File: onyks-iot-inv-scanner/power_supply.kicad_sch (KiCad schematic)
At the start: 16 parts, among them Q1 DMN3150L, Q2 DMN3150L, U1 DW01A, U3 TP4056-42-ESOP8

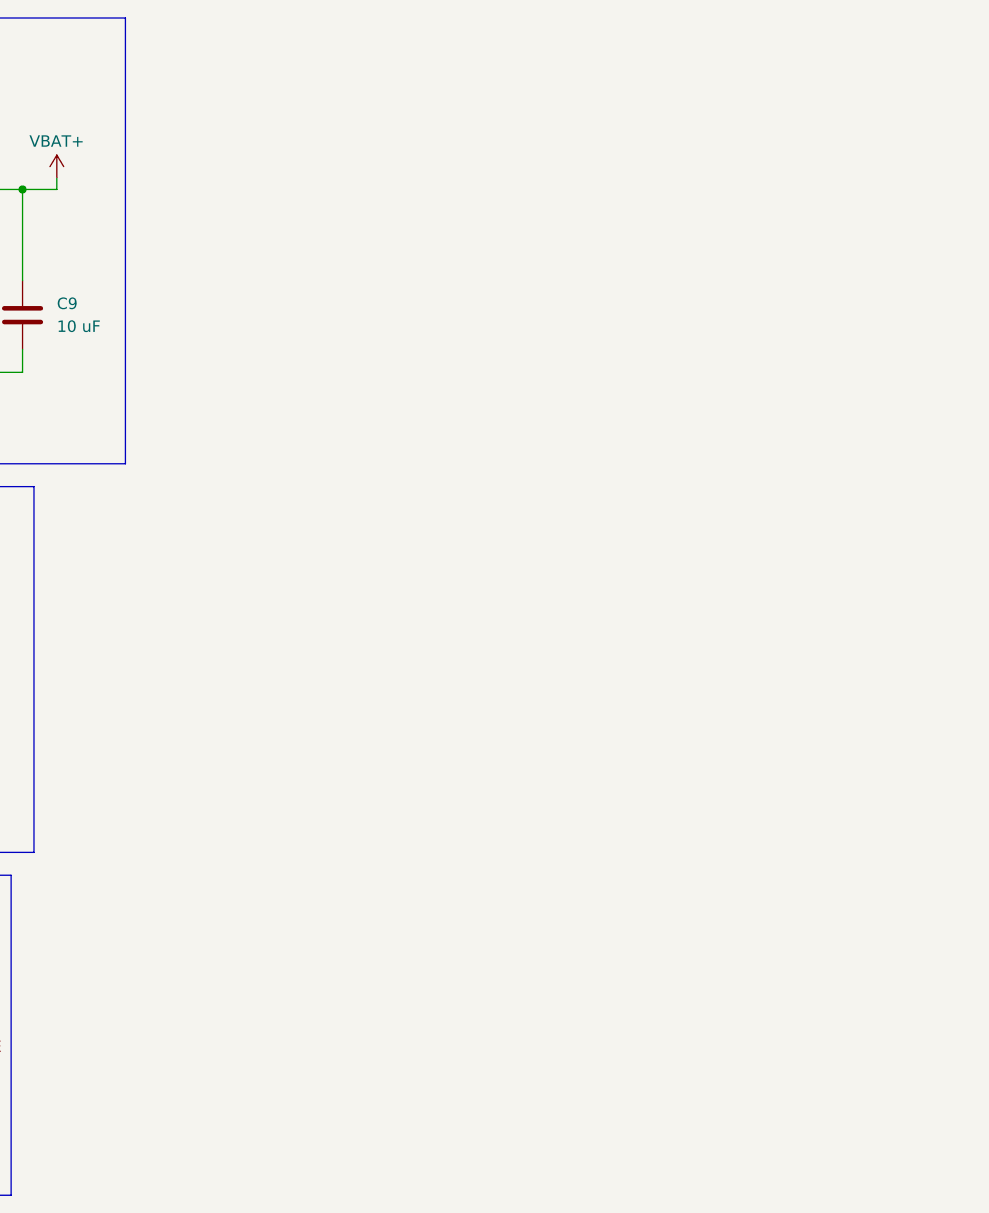
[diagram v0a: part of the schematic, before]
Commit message: added power mux (power switches)
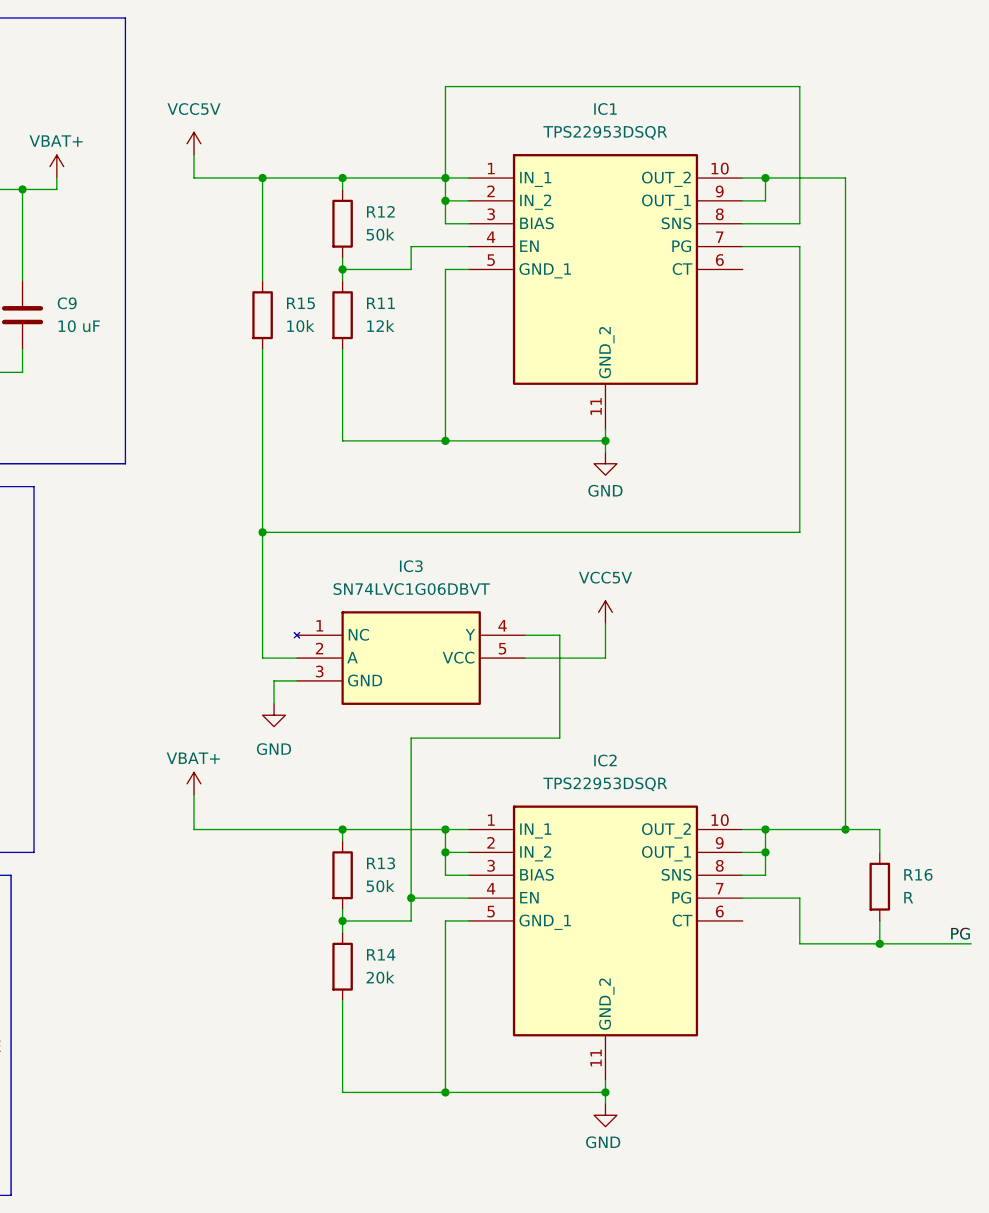
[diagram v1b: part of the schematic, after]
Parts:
- added IC1, IC2: TPS22953DSQR, Samacsys:SON40P200X200X80-11N, symbol Samacsys:TPS22953DSQR
- added IC3: SN74LVC1G06DBVT, Samacsys:SOT95P280X145-5N, symbol Samacsys:SN74LVC1G06DBVT
- added R11: 12k, symbol Device:R
- added R12, R13: 50k, symbol Device:R
- added R14: 20k, symbol Device:R
- added R15: 10k, symbol Device:R
- added R16: R, symbol Device:R
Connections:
- net GND: now also IC1.11 (GND_2), IC1.5 (GND_1), IC2.11 (GND_2), IC2.5 (GND_1), IC3.3 (GND), R11.2, R14.2
- net VBAT+: now also IC2.1 (IN_1), IC2.2 (IN_2), IC2.3 (BIAS), R13.1
- net VCC5V: now also IC1.1 (IN_1), IC1.2 (IN_2), IC1.3 (BIAS), IC1.8 (SNS), IC3.5 (VCC), R12.1, R15.1
- new net: IC1.7 (PG), IC3.2 (A), R15.2
- new net: IC2.4 (EN), IC3.4 (Y), R13.2, R14.1
- new net: IC1.10 (OUT_2), IC1.9 (OUT_1), IC2.10 (OUT_2), IC2.8 (SNS), IC2.9 (OUT_1), R16.1
- new net: IC1.4 (EN), R11.1, R12.2
- new net PG: IC2.7 (PG), R16.2

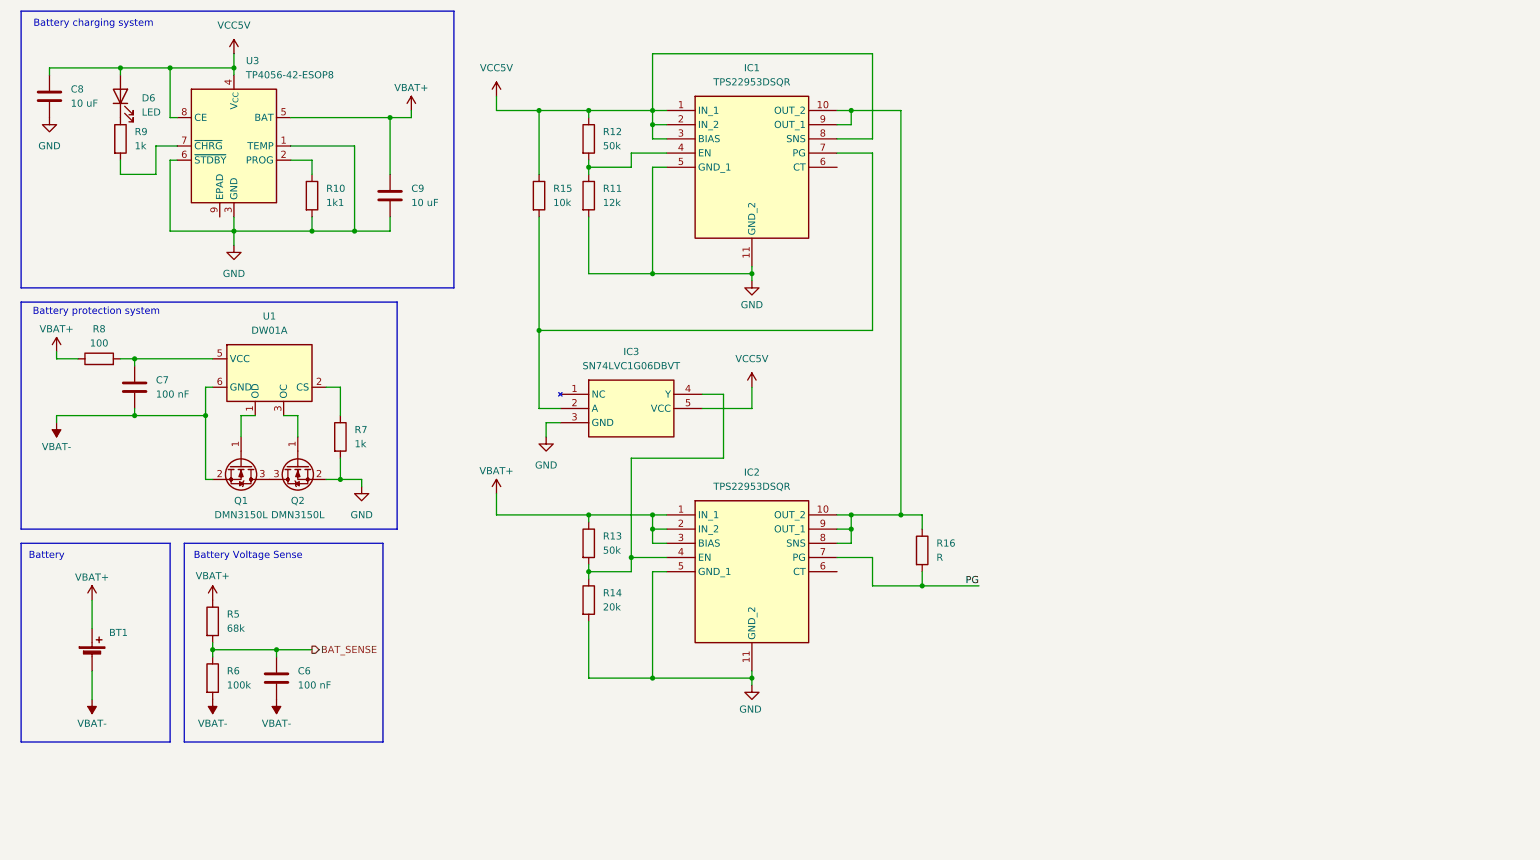
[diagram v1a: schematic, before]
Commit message: added 3v3 dc-dc converter
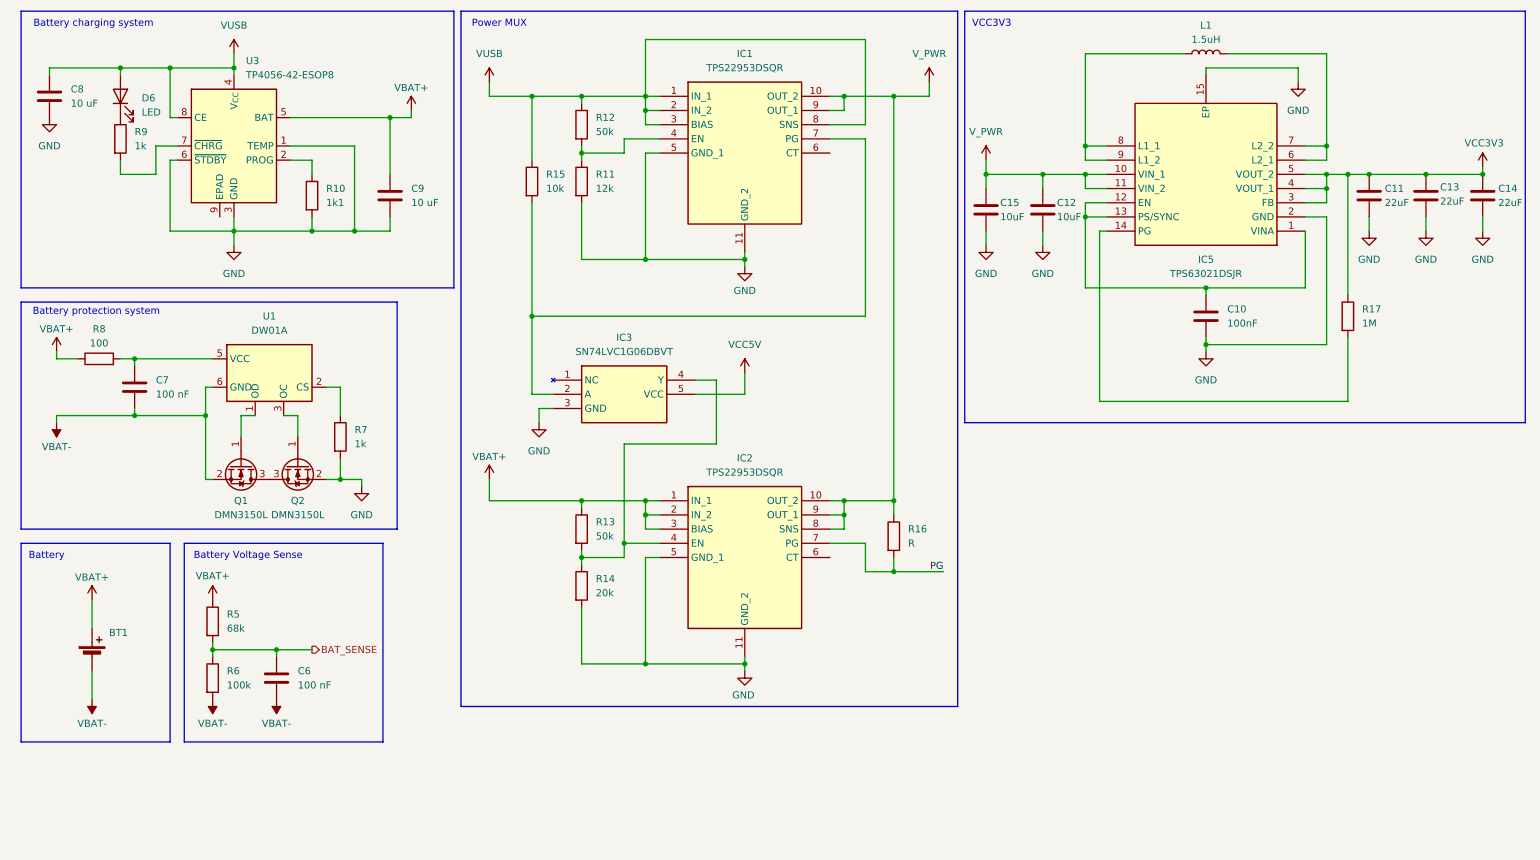
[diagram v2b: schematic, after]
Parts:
- added C10: 100nF, symbol Device:C
- added C11, C13, C14: 22uF, symbol Device:C
- added C12, C15: 10uF, symbol Device:C
- added IC5: TPS63021DSJR, Samacsys:SON50P300X400X100-15N-D, symbol Samacsys:TPS63021DSJR
- added L1: 1.5uH, symbol Device:L
- added R17: 1M, symbol Device:R
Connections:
- net GND: now also C10.2, C11.2, C12.2, C13.2, C14.2, C15.2, IC5.15 (EP), IC5.2 (GND)
- net VCC5V: no longer C8.1, D6.2 (A), IC1.1 (IN_1), IC1.2 (IN_2), IC1.3 (BIAS), IC1.8 (SNS), R12.1, R15.1, U3.4 (V_{CC}), U3.8 (CE)
- net V_PWR: now reaches IC1.10 (OUT_2), IC1.9 (OUT_1), IC2.10 (OUT_2), IC2.8 (SNS), IC2.9 (OUT_1), R16.1
- net V_PWR: now also C12.1, C15.1, IC5.10 (VIN_1), IC5.11 (VIN_2)
- new net: C10.1, IC5.1 (VINA), IC5.12 (EN), IC5.13 (PS/SYNC)
- new net: IC5.14 (PG), R17.2
- new net: IC5.6 (L2_1), IC5.7 (L2_2), L1.2
- new net: IC5.8 (L1_1), IC5.9 (L1_2), L1.1
- new net VCC3V3: C11.1, C13.1, C14.1, IC5.3 (FB), IC5.4 (VOUT_1), IC5.5 (VOUT_2), R17.1
- new net VUSB: C8.1, D6.2 (A), IC1.1 (IN_1), IC1.2 (IN_2), IC1.3 (BIAS), IC1.8 (SNS), R12.1, R15.1, U3.4 (V_{CC}), U3.8 (CE)
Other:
- note added: "Power MUX"
- note added: "VCC3V3"
- moved on the sheet: IC1, IC2, IC3, R11, R12, R13, R14, R15, R16

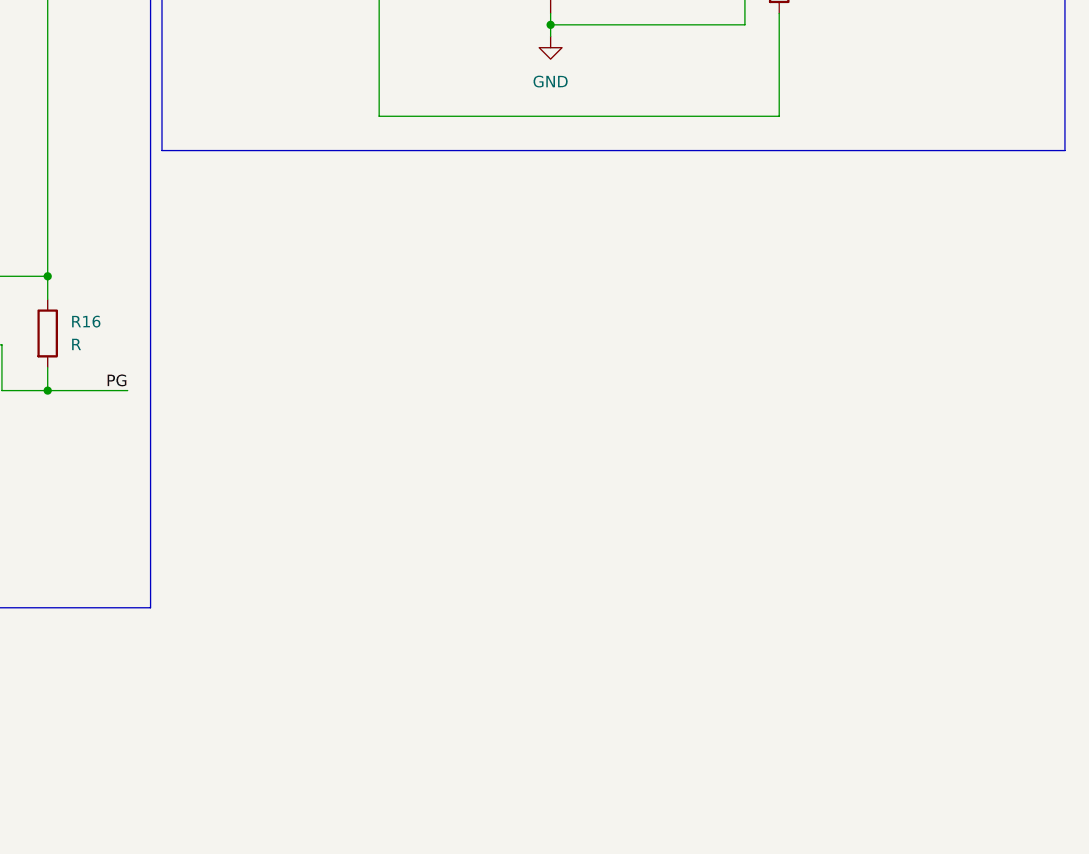
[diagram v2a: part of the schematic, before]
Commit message: created voltage supplies for camera
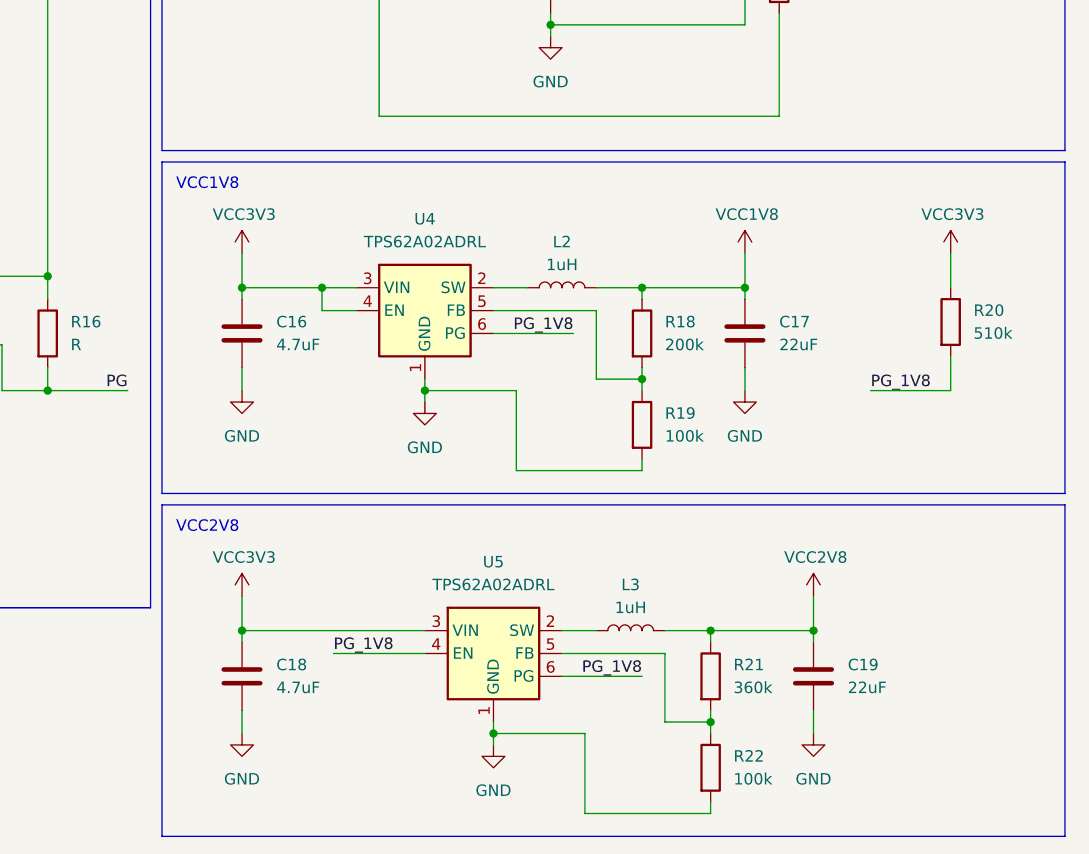
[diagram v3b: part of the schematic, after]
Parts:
- added C16, C18: 4.7uF, symbol Device:C
- added C17, C19: 22uF, symbol Device:C
- added L2, L3: 1uH, symbol Device:L
- added R18: 200k, symbol Device:R
- added R19, R22: 100k, symbol Device:R
- added R20: 510k, symbol Device:R
- added R21: 360k, symbol Device:R
- added U4, U5: TPS62A02ADRL, Package_TO_SOT_SMD:SOT-563, symbol Regulator_Switching:TPS62A02ADRL
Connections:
- net GND: now also C16.2, C17.2, C18.2, C19.2, R19.2, R22.2, U4.1 (GND), U5.1 (GND)
- net VCC3V3: now also C16.1, C18.1, R20.1, U4.3 (VIN), U4.4 (EN), U5.3 (VIN)
- new net: R18.2, R19.1, U4.5 (FB)
- new net: R21.2, R22.1, U5.5 (FB)
- new net: L3.1, U5.2 (SW)
- new net: L2.1, U4.2 (SW)
- new net PG_1V8: R20.2, U4.6 (PG), U5.4 (EN), U5.6 (PG)
- new net VCC1V8: C17.1, L2.2, R18.1
- new net VCC2V8: C19.1, L3.2, R21.1
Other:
- note added: "VCC1V8"
- note added: "VCC2V8"
